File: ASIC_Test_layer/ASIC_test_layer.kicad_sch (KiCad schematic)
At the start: 20 parts, among them J100 MOLEX-524653071, J200 MOLEX-533073071, J5 5024262030, J6 MOLEX-533073071, J7 MOLEX-524653071, P11 Header 11X2, P12 Header 11X2, P13 Header 11X2

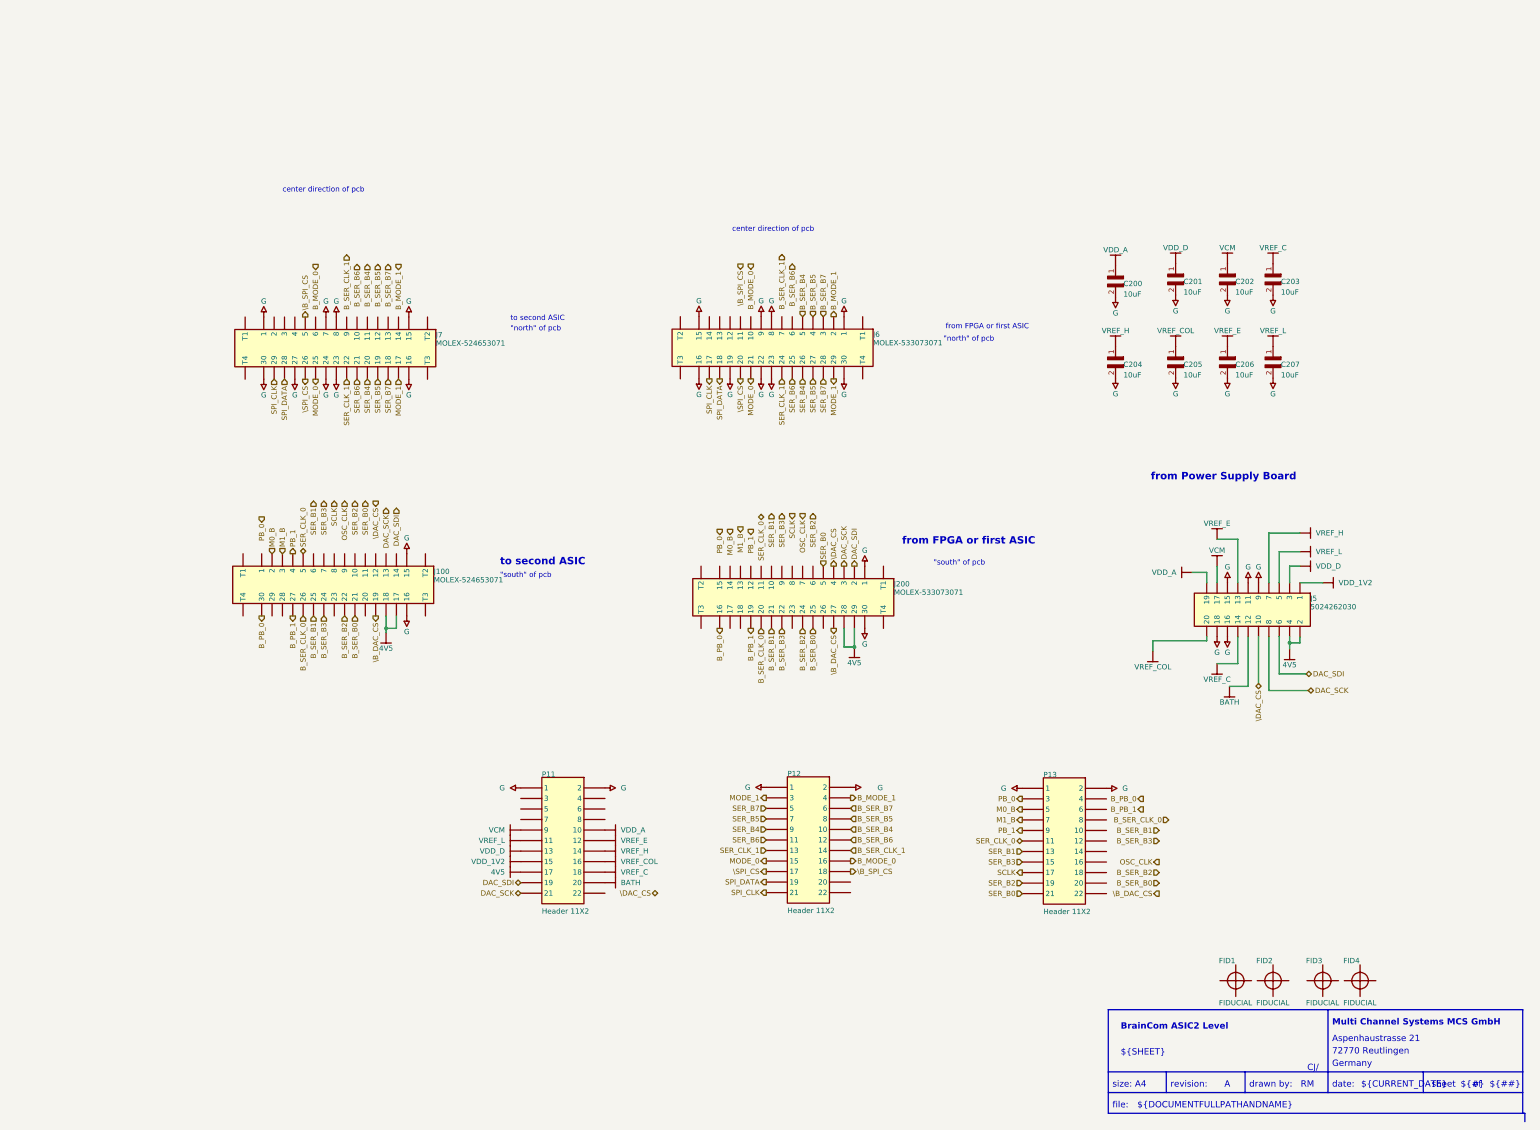
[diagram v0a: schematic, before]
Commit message: fixed test layer
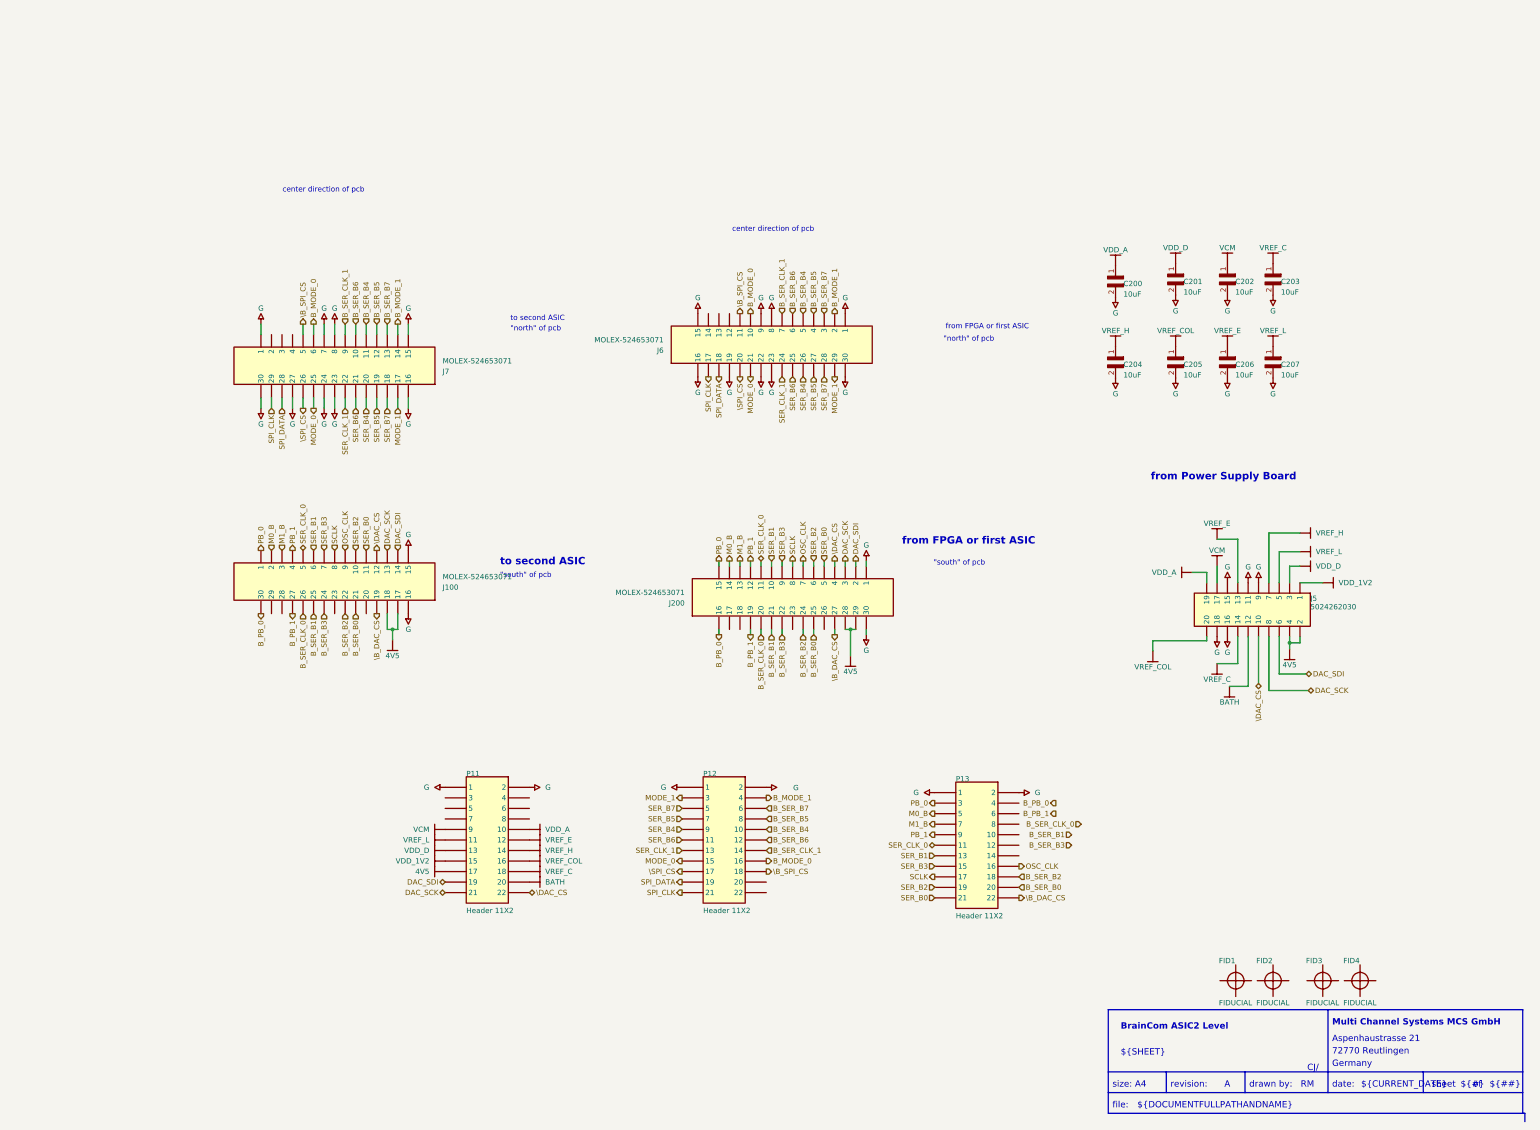
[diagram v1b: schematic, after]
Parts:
- removed J100, J7: MOLEX-524653071, J524653071, symbol TestLayer_RevB-altium-import:root_2_mirrored_MOLEX-5009130302
- removed J200, J6: MOLEX-533073071, J533073071, symbol TestLayer_RevB-altium-import:root_2_MOLEX-5017450301
- added J100, J200, J6, J7: MOLEX-524653071, FDM_footprints:J524653071_Board2Board, symbol FDM_project_Library:Board2Board_MOLEX-5009130302_1_1
- C200, C201, C202, C203, C204, C205, C206, C207: footprint CAPC1709X50N -> Footprints:CAPC1709X50N
- FID1, FID2, FID3, FID4: footprint MFID0508 -> Footprints:MFID0508
- J5: footprint JMOLEX-0559090274V1 -> Footprints:JMOLEX-0559090274V1
- P11, P12, P13: footprint HDR2X11 -> Footprints:HDR2X11
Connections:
- net 4V5: now also J100.17, J100.18, J200.28, J200.29
- net B_MODE_0: now also J6.10, J7.6
- net B_MODE_1: now also J6.2, J7.14
- net B_PB_0: now also J100.30, J200.16
- net B_PB_1: now also J100.27, J200.19
- net B_SER_B0: now also P13.20, J100.21, J200.25
- net B_SER_B1: now also J100.25, J200.21
- net B_SER_B2: now also P13.18, J100.22, J200.24
- net B_SER_B3: now also J100.24, J200.22
- net B_SER_B4: now also J6.5, J7.11
- net B_SER_B5: now also J6.4, J7.12
- net B_SER_B6: now also J6.6, J7.10
- net B_SER_B7: now also J6.3, J7.13
- net B_SER_CLK_0: now also J100.26, J200.20
- net B_SER_CLK_1: now also J6.7, J7.9
- net DAC_SCK: now also J100.13, J200.3
- net DAC_SDI: now also J100.14, J200.2
- net G: now also J100.15, J100.16, J200.1, J200.30, J6.1, J6.15, J6.16, J6.19, J6.22, J6.23, J6.30, J6.8, J6.9, J7.1, J7.15, J7.16, J7.23, J7.24, J7.27, J7.30, J7.7, J7.8
- net M0_B: now also J100.2, J200.14
- net M1_B: now also J100.3, J200.13
- net MODE_0: now also J6.21, J7.25
- net MODE_1: now also J6.29, J7.17
- net OSC_CLK: now also P13.16, J100.9, J200.7
- net PB_0: now also J100.1, J200.15
- net PB_1: now also J100.4, J200.12
- net SCLK: now also J100.8, J200.8
- net SER_B0: now also J100.11, J200.5
- net SER_B1: now also J100.6, J200.10
- net SER_B2: now also J100.10, J200.6
- net SER_B3: now also J100.7, J200.9
- net SER_B4: now also J6.26, J7.20
- net SER_B5: now also J6.27, J7.19
- net SER_B6: now also J6.25, J7.21
- net SER_B7: now also J6.28, J7.18
- net SER_CLK_0: now also J100.5, J200.11
- net SER_CLK_1: now also J6.24, J7.22
- net SPI_CLK: now also J6.17, J7.29
- net SPI_DATA: now also J6.18, J7.28
- net \B_DAC_CS: now also P13.22, J100.19, J200.27
- net \B_SPI_CS: now also J6.11, J7.5
- net \DAC_CS: now also P11.22, J100.12, J200.4
- net \SPI_CS: now also J6.20, J7.26
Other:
- moved on the sheet: P11, P12, P13

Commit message: Test Commint
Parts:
- added IC1: DS90UB914ATRHSJQ1, Samacsys:QFN50P700X700X80-49N, symbol Samacsys_new:DS90UB914ATRHSJQ1
- added U1: DS90UB913ATRTVTQ1, Samacsys:QFN50P500X500X80-33N, symbol Samacsys_new:DS90UB913ATRTVTQ1
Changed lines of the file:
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@@
+    )
+  )
+  (symbol (lib_id "Samacsys_new:DS90UB914ATRHSJQ1") (at 22.86 45.72 0) (unit 1)
+    (in_bom yes) (on_board yes) (dnp no) (fields_autoplaced)
+    (property "Reference" "IC1" (at 74.93 38.7919 0)
+      (effects (font (size 1.27 1.27)))
+    )
+    (property "Value" "DS90UB914ATRHSJQ1" (at 74.93 41.3319 0)
+      (effects (font (size 1.27 1.27)))
+    )
+    (property "Footprint" "Samacsys:QFN50P700X700X80-49N" (at 64.77 127.94 0)
+      (effects (font (size 1.27 1.27)) (justify left top) hide)
+    )
+    (property "Datasheet" "http://www.ti.com/lit/gpn/ds90ub914a-q1" (at 64.77 227.94 0)
+      (effects (font (size 1.27 1.27)) (justify left top) hide)
+    )
+    (property "Height" "0.8" (at 64.77 427.94 0)
+      (effects (font (size 1.27 1.27)) (justify left top) hide)
+    )
+    (property "Manufacturer_Name" "Texas Instruments" (at 64.77 527.94 0)
+      (effects (font (size 1.27 1.27)) (justify left top) hide)
+    )
+    (property "Manufacturer_Part_Number" "DS90UB914ATRHSJQ1" (at 64.77 627.94 0)
+      (effects (font (size 1.27 1.27)) (justify left top) hide)
+    )
+    (property "Mouser Part Number" "595-S90UB914ATRHSJQ1" (at 64.77 727.94 0)
+      (effects (font (size 1.27 1.27)) (justify left top) hide)
+    )
+    (property "Mouser Price/Stock" "https://www.mouser.co.uk/ProductDetail/Texas-Instruments/DS90UB914ATRHSJQ1?qs=fi7yB2oewZkYA4VUeypQnA%3D%3D" (at 64.77 827.94 0)
+      (effects (font (size 1.27 1.27)) (justify left top) hide)
+    )
+    (property "Arrow Part Number" "DS90UB914ATRHSJQ1" (at 64.77 927.94 0)
+      (effects (font (size 1.27 1.27)) (justify left top) hide)
+    )
+    (property "Arrow Price/Stock" "https://www.arrow.com/en/products/ds90ub914atrhsjq1/texas-instruments?region=nac" (at 64.77 1027.94 0)
+      (effects (font (size 1.27 1.27)) (justify left top) hide)
+    )
+    (pin "30")
+    (pin "35")
+    (pin "38")
+    (pin "49")
+    (pin "6")
+    (pin "28")
+    (pin "13")
+    (pin "37")
+    (pin "36")
+    (pin "33")
+    (pin "8")
+    (pin "24")
+    (pin "25")
+    (pin "12")
+    (pin "9")
+    (pin "32")
+    (pin "34")
+    (pin "7")
+    (pin "31")
+    (pin "2")
+    (pin "4")
+    (pin "42")
+    (pin "27")
+    (pin "19")
+    (pin "47")
+    (pin "48")
+    (pin "43")
+    (pin "40")
+    (pin "45")
+    (pin "18")
+    (pin "17")
+    (pin "14")
+    (pin "23")
+    (pin "1")
+    (pin "29")
+    (pin "11")
+    (pin "5")
+    (pin "22")
+    (pin "41")
+    (pin "16")
+    (pin "26")
+    (pin "44")
+    (pin "3")
+    (pin "20")
+    (pin "39")
+    (pin "10")
+    (pin "15")
+    (pin "46")
+    (pin "21")
+    (instances
+      (project "ASIC_test_layer"
+        (path "/a9e8b88f-ed72-4a5f-81ca-16c1b71d95c2"
+          (reference "IC1") (unit 1)
+        )
+      )
     )
   )
@@
         )
       )
+    )
+  )
+  (symbol (lib_id "Samacsys_new:DS90UB913ATRTVTQ1") (at 24.13 125.73 0) (unit 1)
+    (in_bom yes) (on_board yes) (dnp no) (fields_autoplaced)
+    (property "Reference" "U1" (at 71.12 118.8019 0)
+      (effects (font (size 1.27 1.27)))
+    )
+    (property "Value" "DS90UB913ATRTVTQ1" (at 71.12 121.3419 0)
+      (effects (font (size 1.27 1.27)))
+    )
+    (property "Footprint" "Samacsys:QFN50P500X500X80-33N" (at 60.96 210.49 0)
+      (effects (font (size 1.27 1.27)) (justify left top) hide)
+    )
+    (property "Datasheet" "http://www.ti.com/lit/gpn/ds90ub913a-q1" (at 60.96 310.49 0)
+      (effects (font (size 1.27 1.27)) (justify left top) hide)
+    )
+    (property "Height" "0.8" (at 60.96 510.49 0)
+      (effects (font (size 1.27 1.27)) (justify left top) hide)
+    )
+    (property "Manufacturer_Name" "Texas Instruments" (at 60.96 610.49 0)
+      (effects (font (size 1.27 1.27)) (justify left top) hide)
+    )
+    (property "Manufacturer_Part_Number" "DS90UB913ATRTVTQ1" (at 60.96 710.49 0)
+      (effects (font (size 1.27 1.27)) (justify left top) hide)
+    )
+    (property "Mouser Part Number" "595-S90UB913ATRTVTQ1" (at 60.96 810.49 0)
+      (effects (font (size 1.27 1.27)) (justify left top) hide)
+    )
+    (property "Mouser Price/Stock" "https://www.mouser.co.uk/ProductDetail/Texas-Instruments/DS90UB913ATRTVTQ1?qs=v3HA%252BRzKb3dFl1noSy3g8g%3D%3D" (at 60.96 910.49 0)
+      (effects (font (size 1.27 1.27)) (justify left top) hide)
+    )
+    (property "Arrow Part Number" "DS90UB913ATRTVTQ1" (at 60.96 1010.49 0)
+      (effects (font (size 1.27 1.27)) (justify left top) hide)
+    )
+    (property "Arrow Price/Stock" "https://www.arrow.com/en/products/ds90ub913atrtvtq1/texas-instruments?region=nac" (at 60.96 1110.49 0)
+      (effects (font (size 1.27 1.27)) (justify left top) hide)
+    )
+    (pin "30")
+    (pin "24")
+    (pin "5")
+    (pin "22")
+    (pin "26")
+    (pin "9")
+    (pin "21")
+    (pin "3")
+    (pin "4")
+    (pin "23")
+    (pin "33")
+    (pin "19")
+    (pin "16")
+    (pin "28")
+    (pin "20")
+    (pin "10")
+    (pin "14")
+    (pin "17")
+    (pin "2")
+    (pin "6")
+    (pin "8")
+    (pin "7")
+    (pin "31")
+    (pin "27")
+    (pin "25")
+    (pin "32")
+    (pin "18")
+    (pin "29")
+    (pin "13")
+    (pin "12")
+    (pin "1")
+    (pin "11")
+    (pin "15")
+    (instances
+      (project "ASIC_test_layer"
+        (path "/a9e8b88f-ed72-4a5f-81ca-16c1b71d95c2"
+          (reference "U1") (unit 1)
+        )
+      )
